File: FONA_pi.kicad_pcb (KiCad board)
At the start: 2 copper layers, 101.6 x 68.6 mm, 21 parts, among them J1 Conn_01x20_Socket, J10 Conn_01x04_Pin, J11 Conn_01x20_Socket, J12 Conn_01x20_Socket, J2 Conn_02x20_Odd_Even, J3 Conn_01x20_Socket, J4 Conn_01x20_Socket, J5 Conn_01x18, J6 Conn_01x18_Socket, J7 Conn_01x20_Socket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

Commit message: Made a bunch of warning fixes.  Silkscreen lettering, etc
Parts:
- moved J5 0.76 mm to (148.0, 65.1)
- moved J4 0.11 mm to (119.9, 61.0)
- moved J7 0.11 mm to (116.2, 61.0)
- moved J3 0.11 mm to (112.6, 61.0)
- moved J8 0.10 mm to (157.8, 65.1)
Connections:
- J10 pad 3: unconnected-(J10-Pin_3-Pad3) -> Net-(J1-Pin_1)
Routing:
- net Net-(J1-Pin_1): track 15.8 -> 69.4 mm
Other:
- board text added: "GPIO 0 EEPROM SDA"
- board text added: "GPIO 10 SPI0 MOSI"
- board text added: "GPIO 11 SPI0 SCLK"
- board text added: "GPIO 12 PWM0"
- board text added: "GPIO 13 PWM1"
- board text added: "GPIO 14 UART TX"
- board text added: "GPIO 15 UART RX"
- board text added: "GPIO 18 PCM CLK"
- board text added: "GPIO 19 PCM FS"
- board text added: "GPIO 2 I2C1 SDA"
- board text added: "GPIO 20 PCM DIN"
- board text added: "GPIO 21 PCM DOUT"
- board text added: "GPIO 3 I2C1 SCL"
- board text added: "GPIO 4 GPCLK0"
- board text added: "GPIO 7 SPI0 CE1"
- board text added: "GPIO 8 SPI0 CE0"
- board text added: "GPIO 9 SPI0 MISO"
- board text removed: "GPIO 0 (EEPROM SDA)"
- board text removed: "GPIO 10 (SPI0 MOSI)"
- board text removed: "GPIO 11 (SPI0 SCLK)"
- board text removed: "GPIO 12 (PWM0)"
- board text removed: "GPIO 13 (PWM1)"
- board text removed: "GPIO 14 (UART TX)"
- board text removed: "GPIO 15 (UART RX)"
- board text removed: "GPIO 18 (PCM CLK)"
- board text removed: "GPIO 19 (PCM FS)"
- board text removed: "GPIO 2 (I2C1 SDA)"
- board text removed: "GPIO 20 (PCM DIN)"
- board text removed: "GPIO 21 (PCM DOUT)"
- board text removed: "GPIO 3 (I2C1 SCL)"
- board text removed: "GPIO 4 (GPCLK0)"
- board text removed: "GPIO 7 (SPI0 CE1)"
- board text removed: "GPIO 8 (SPI0 CE0)"
- board text removed: "GPIO 9 (SPI0 MISO)"

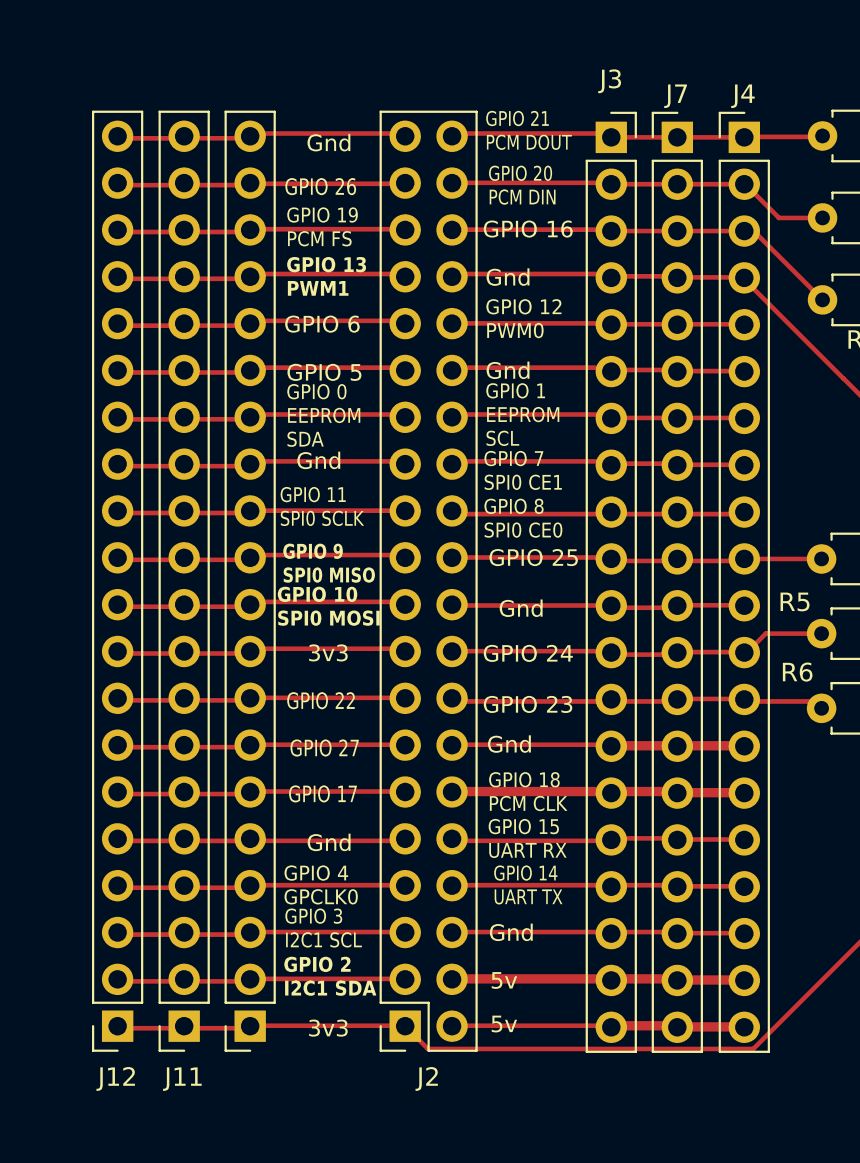
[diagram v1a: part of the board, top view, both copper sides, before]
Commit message: Added fat tracks to the Pi prototyping area
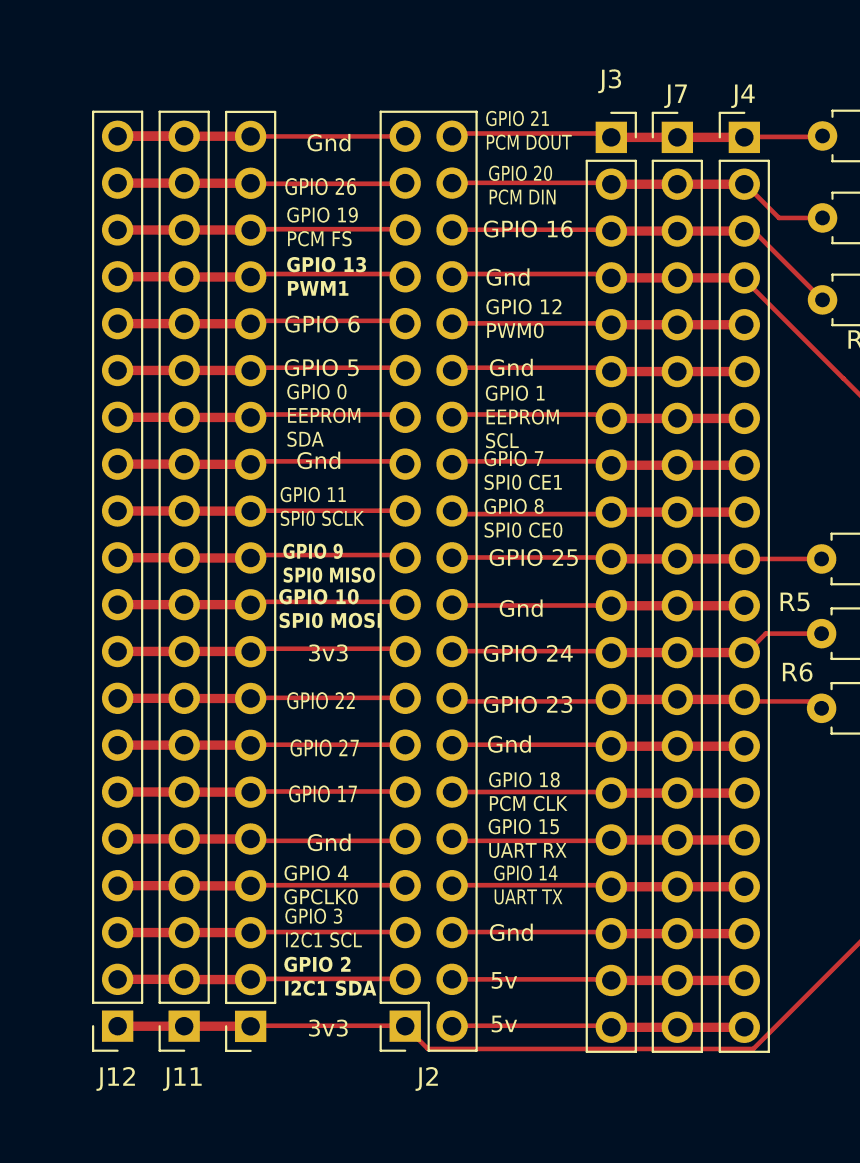
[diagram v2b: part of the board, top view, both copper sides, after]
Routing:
- net Net-(J1-Pin_20): track 15.8 -> 22.8 mm

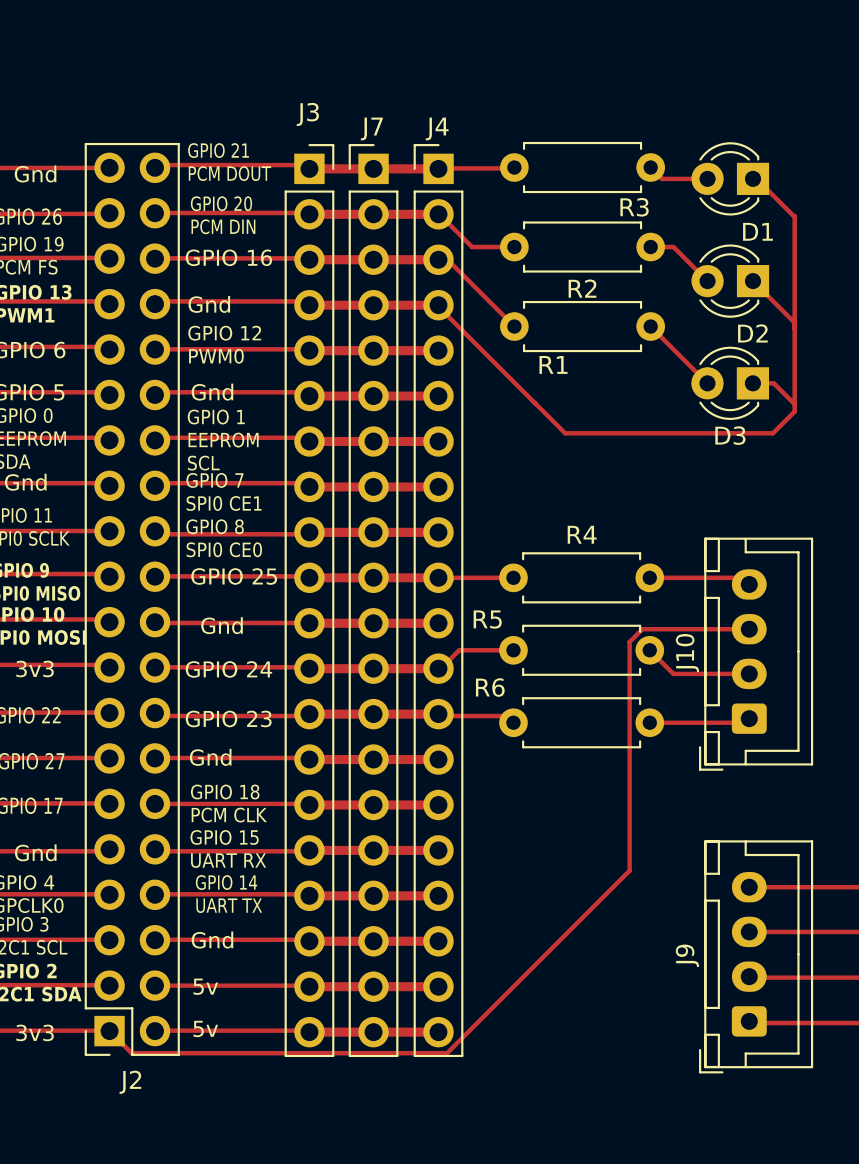
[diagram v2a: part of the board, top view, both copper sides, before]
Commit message: Added rectangles in mask.  Exposes tracks as desired, but tons of errors
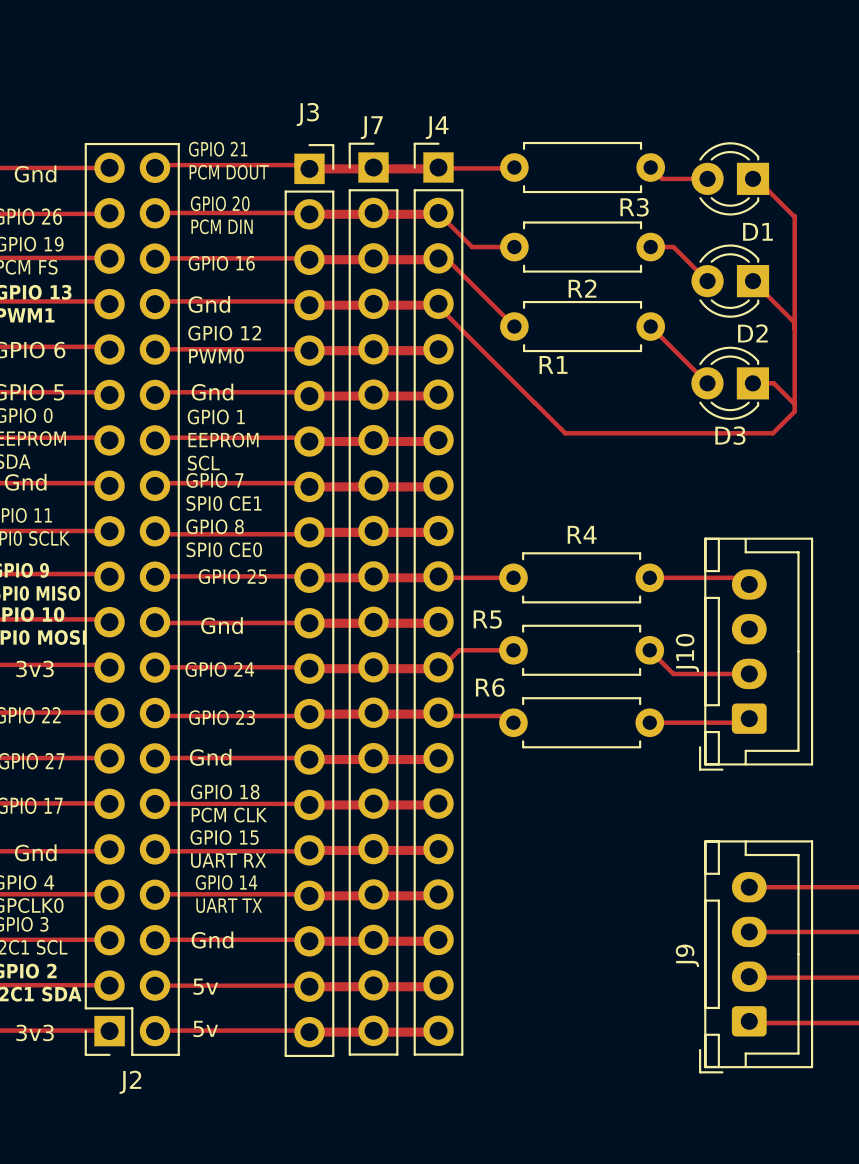
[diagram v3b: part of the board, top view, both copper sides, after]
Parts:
- moved J4 0.08 mm to (119.9, 60.9)
- moved J7 0.08 mm to (116.2, 60.9)
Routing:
- net Net-(J1-Pin_1): track 69.4 -> 15.9 mm
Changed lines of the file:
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@@
   )
   (footprint "Connector_PinHeader_2.54mm:PinHeader_1x20_P2.54mm_Vertical" (layer "F.Cu")
-    (at 119.8626 60.96)
+    (at 119.8626 60.8838)
     (descr "Through hole straight pin header, 1x20, 2.54mm pitch, single row")
     (tags "Through hole pin header THT 1x20 2.54mm single row")
@@
   )
   (footprint "Connector_PinHeader_2.54mm:PinHeader_1x20_P2.54mm_Vertical" (layer "F.Cu")
-    (at 116.2304 60.96)
+    (at 116.2304 60.8838)
     (descr "Through hole straight pin header, 1x20, 2.54mm pitch, single row")
     (tags "Through hole pin header THT 1x20 2.54mm single row")
@@
     )
   )
+  (gr_rect (start 111.9124 60.1218) (end 120.6246 110.1852)
+    (stroke (width 0.2) (type solid)) (fill solid) (layer "F.Mask"))
+  (gr_rect (start 84.9376 59.8678) (end 93.9292 110.0074)
+    (stroke (width 0.15) (type solid)) (fill solid) (layer "F.Mask"))
   (gr_rect (start 83.8708 59.2582) (end 83.947 59.2582)
     (stroke (width 0.15) (type default)) (fill none) (layer "F.Mask"))
@@
   )
   (gr_text "GPIO 20\nPCM DIN" (at 105.9688 64.6938) (layer "F.SilkS")
-    (effects (font (size 0.8001 0.635) (thickness 0.12192)) (justify left bottom))
+    (effects (font (size 0.8001 0.6096) (thickness 0.12192)) (justify left bottom))
   )
   (gr_text "GPIO 11\nSPI0 SCLK" (at 94.6658 82.1182) (layer "F.SilkS")
@@
     (effects (font (size 0.89408 0.89408) (thickness 0.12192)) (justify left))
   )
-  (gr_text "GPIO 16" (at 105.664 65.9638) (layer "F.SilkS")
-    (effects (font (size 0.89408 0.89408) (thickness 0.12192)) (justify left))
+  (gr_text "GPIO 16" (at 105.8418 66.2686) (layer "F.SilkS")
+    (effects (font (size 0.8001 0.6858) (thickness 0.12192)) (justify left))
   )
   (gr_text "-" (at 150.0378 107.7468 -90) (layer "F.SilkS")
@@
   )
   (gr_text "GPIO 24\n" (at 105.664 88.9762) (layer "F.SilkS")
-    (effects (font (size 0.89408 0.89408) (thickness 0.12192)) (justify left))
+    (effects (font (size 0.8001 0.7112) (thickness 0.12192)) (justify left))
   )
   (gr_text "GPIO 14\nUART TX\n" (at 106.2482 102.6414) (layer "F.SilkS")
@@
     (effects (font (size 0.8001 0.7112) (thickness 0.127) bold) (justify left bottom))
   )
-  (gr_text "GPIO 21\nPCM DOUT" (at 105.8164 61.722) (layer "F.SilkS")
-    (effects (font (size 0.8001 0.635) (thickness 0.12192)) (justify left bottom))
+  (gr_text "GPIO 21\nPCM DOUT" (at 105.8672 61.6458) (layer "F.SilkS")
+    (effects (font (size 0.8001 0.6096) (thickness 0.12192)) (justify left bottom))
   )
   (gr_text "3v3" (at 96.167938 109.2962) (layer "F.SilkS")
@@
     (effects (font (size 0.8001 0.7112) (thickness 0.1143)) (justify left))
   )
-  (gr_text "GPIO 23" (at 105.664 91.7448) (layer "F.SilkS")
-    (effects (font (size 0.89408 0.89408) (thickness 0.12192)) (justify left))
+  (gr_text "GPIO 23" (at 105.8672 91.6686) (layer "F.SilkS")
+    (effects (font (size 0.8001 0.6858) (thickness 0.12192)) (justify left))
   )
   (gr_text "Gnd" (at 105.8926 93.9038) (layer "F.SilkS")
     (effects (font (size 0.89408 0.89408) (thickness 0.12192)) (justify left))
   )
-  (gr_text "GPIO 25\n" (at 108.458 84.3026) (layer "F.SilkS")
-    (effects (font (size 0.89408 0.89408) (thickness 0.12192)) (justify bottom))
+  (gr_text "GPIO 25\n" (at 108.3818 84.2518) (layer "F.SilkS")
+    (effects (font (size 0.8001 0.7112) (thickness 0.12192)) (justify bottom))
   )
   (gr_text "TX" (at 149.90064 80.5942) (layer "F.SilkS")
@@
   (segment (start 92.8116 106.5946) (end 101.4476 106.5946) (width 0.25) (layer "F.Cu") (net 1))
   (segment (start 89.4868 106.62) (end 85.8774 106.62) (width 0.508) (layer "F.Cu") (net 1))
-  (segment (start 102.708 110.395) (end 120.349301 110.395) (width 0.25) (layer "F.Cu") (net 2))
   (segment (start 89.4868 109.16) (end 93.0818 109.16) (width 0.508) (layer "F.Cu") (net 2))
   (segment (start 93.0818 109.16) (end 93.091 109.1692) (width 0.508) (layer "F.Cu") (net 2))
-  (segment (start 120.349301 110.395) (end 130.5486 100.195701) (width 0.25) (layer "F.Cu") (net 2))
-  (segment (start 130.5486 87.406609) (end 131.261209 86.694) (width 0.25) (layer "F.Cu") (net 2))
   (segment (start 85.8774 109.16) (end 89.4868 109.16) (width 0.508) (layer "F.Cu") (net 2))
   (segment (start 101.4476 109.1346) (end 92.8116 109.1346) (width 0.25) (layer "F.Cu") (net 2))
-  (segment (start 101.473 109.16) (end 102.708 110.395) (width 0.25) (layer "F.Cu") (net 2))
-  (segment (start 130.5486 100.195701) (end 130.5486 87.406609) (width 0.25) (layer "F.Cu") (net 2))
-  (segment (start 131.261209 86.694) (end 137.2362 86.694) (width 0.25) (layer "F.Cu") (net 2))
+  (segment (start 101.473 109.16) (end 101.5238 109.2108) (width 0.25) (layer "F.Cu") (net 2))
   (segment (start 93.091 101.5492) (end 89.496 101.5492) (width 0.508) (layer "F.Cu") (net 3))
   (segment (start 89.496 101.5492) (end 89.4868 101.54) (width 0.508) (layer "F.Cu") (net 3))

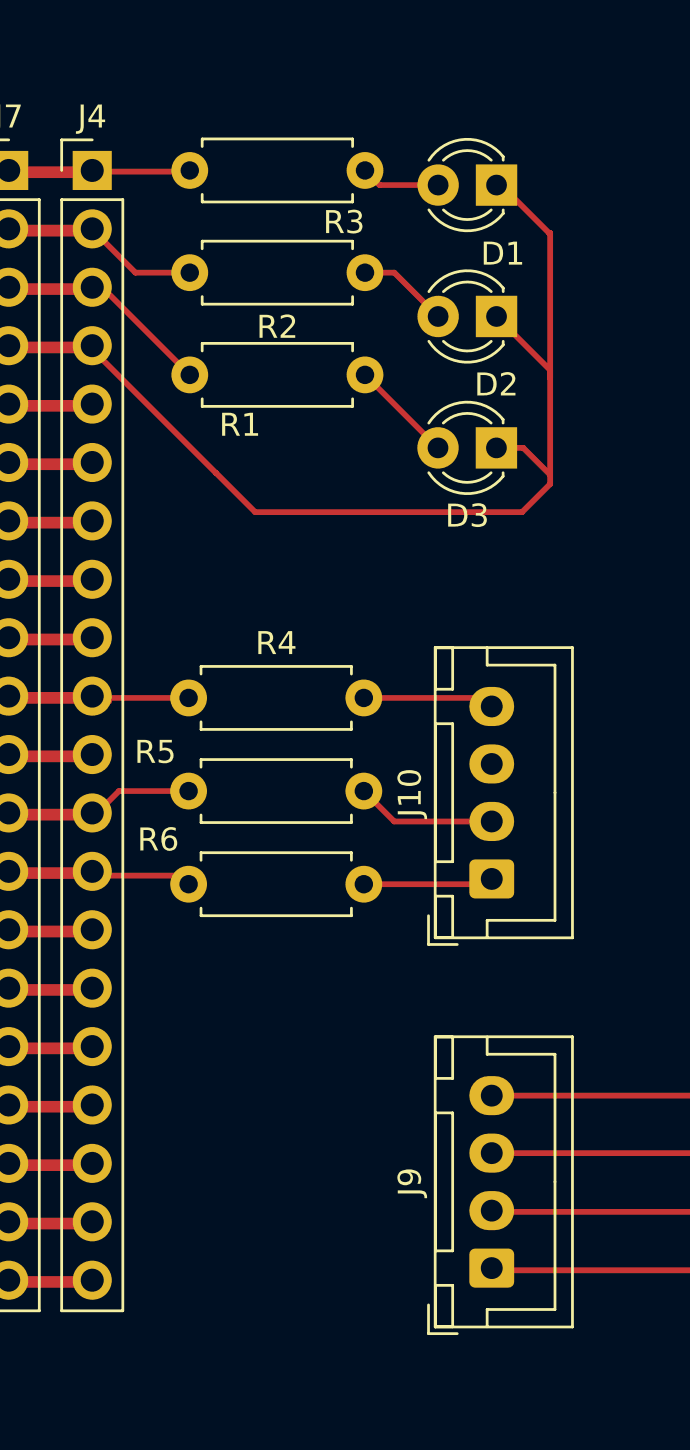
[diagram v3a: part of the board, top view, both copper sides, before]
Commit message: Added isolated proto area
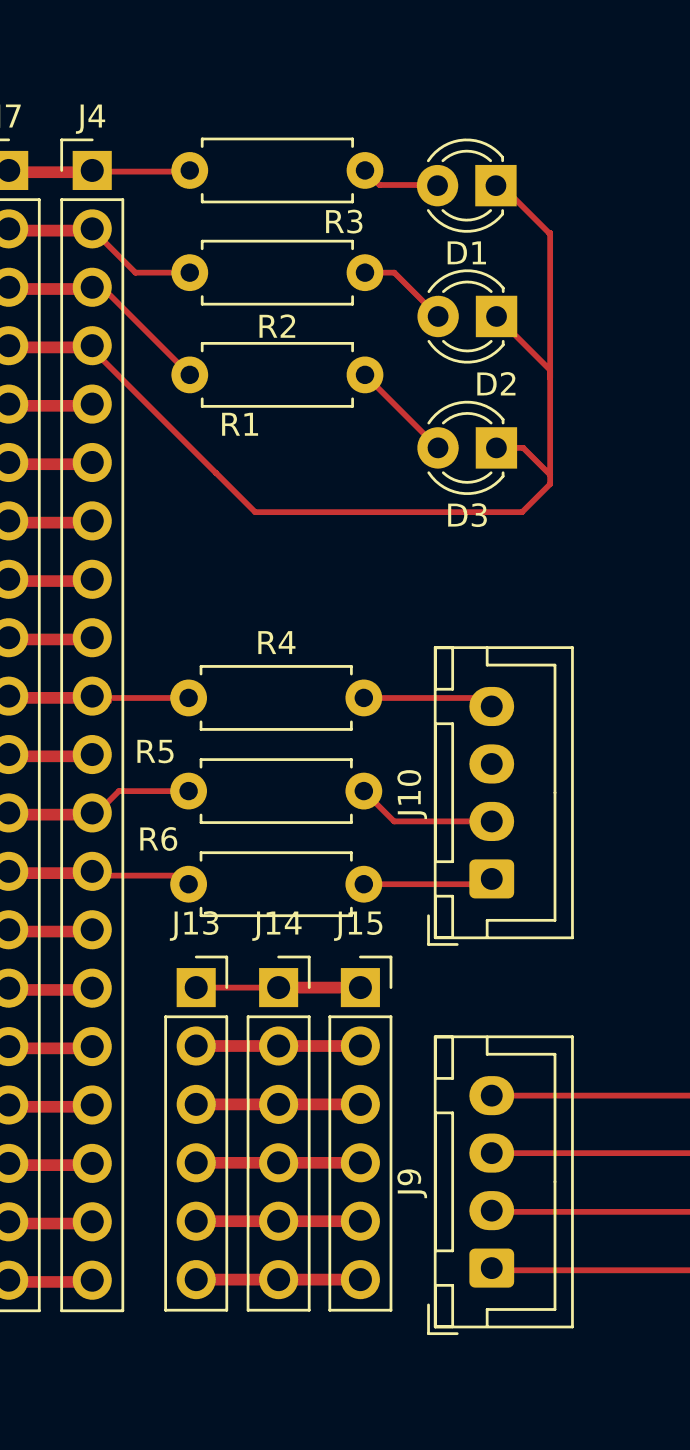
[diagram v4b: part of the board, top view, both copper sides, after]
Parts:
- added J13: Conn_01x06_Socket, Connector_PinSocket_2.54mm:PinSocket_1x06_P2.54mm_Vertical, F.Cu at (124.4, 96.4)
- added J14: Conn_01x06_Socket, Connector_PinSocket_2.54mm:PinSocket_1x06_P2.54mm_Vertical, F.Cu at (128.0, 96.4)
- added J15: Conn_01x06_Socket, Connector_PinSocket_2.54mm:PinSocket_1x06_P2.54mm_Vertical, F.Cu at (131.5, 96.4)
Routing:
- net Net-(J13-Pin_1): track 15.9 -> 23.2 mm
- net Net-(J13-Pin_5): track 15.9 -> 23.1 mm
- net Net-(J13-Pin_6): track 15.8 -> 23.0 mm
- net Net-(J13-Pin_4): track 15.8 -> 23.0 mm
- net Net-(J13-Pin_3): track 15.8 -> 23.0 mm
- net Net-(J13-Pin_2): track 15.8 -> 23.0 mm
